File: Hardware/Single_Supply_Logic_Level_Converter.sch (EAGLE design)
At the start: 33 parts, among them U1 TXB0104, U2 TPS61200, U3 ADJ

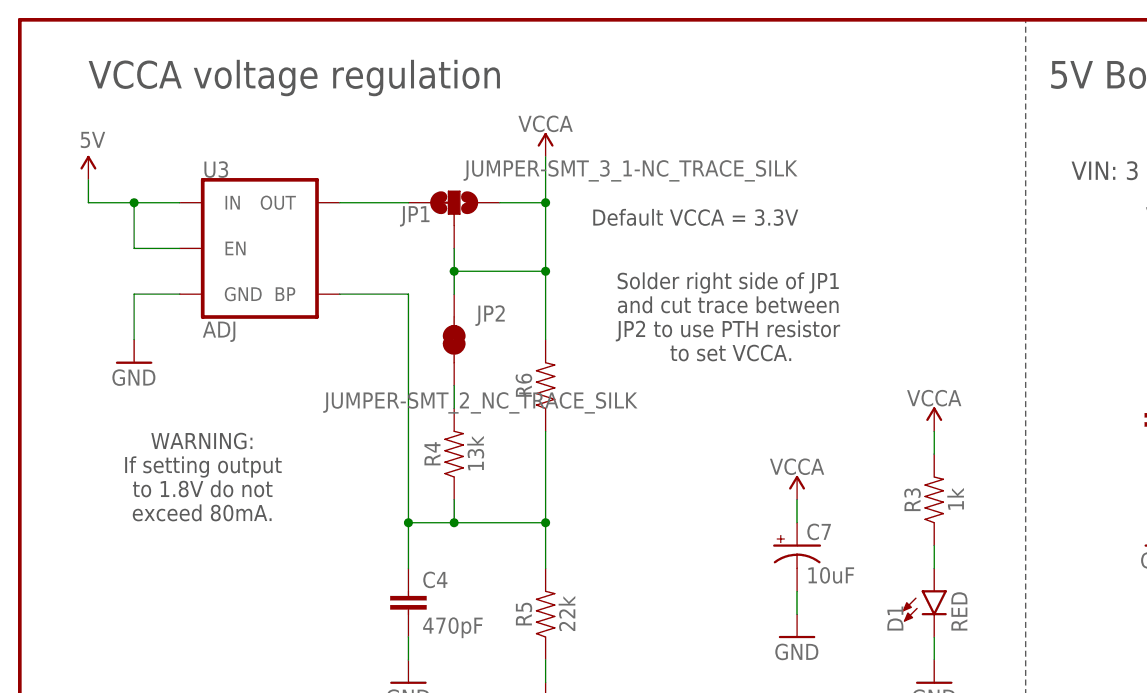
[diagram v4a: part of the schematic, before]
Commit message: changing voltage output programming
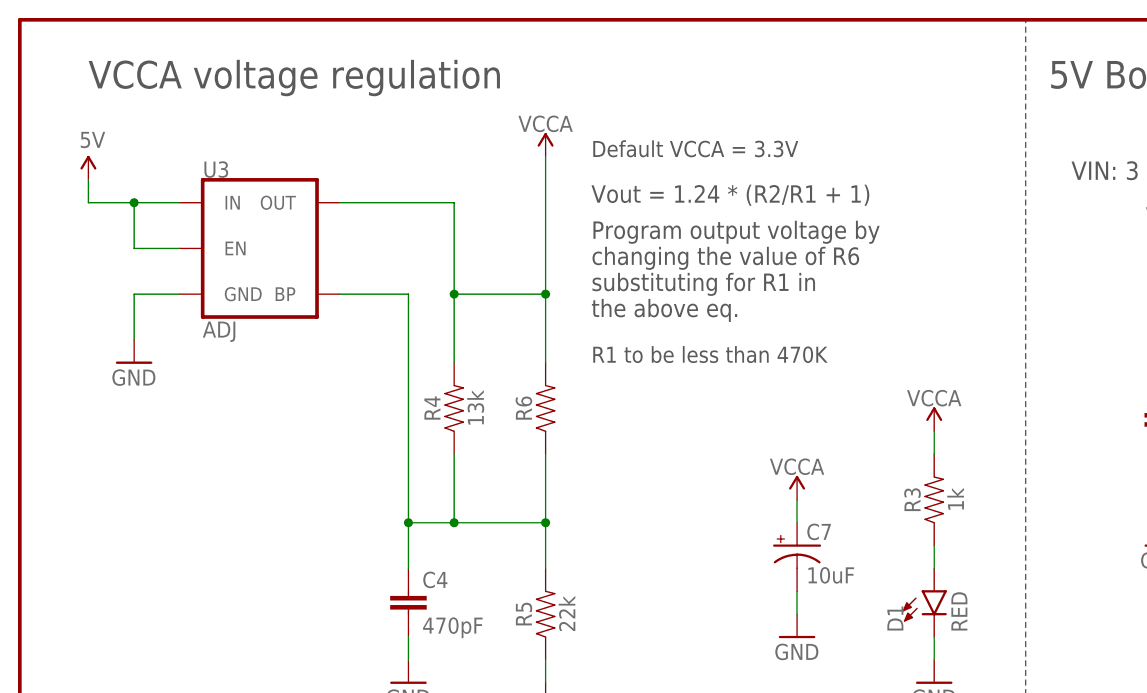
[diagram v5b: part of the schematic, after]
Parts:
- removed JP1: JUMPER-SMT_3_1-NC_TRACE_SILK, SparkFun-Jumpers:JUMPER-SMT_3_1-NC_TRACE_SILK
- removed JP2: JUMPER-SMT_2_NC_TRACE_SILK, SparkFun-Jumpers:JUMPER-SMT_2_NC_TRACE_SILK
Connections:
- removed net N$1: JP1.3, U3.OUT
- removed net N$12: JP2.1, R4.2
- net VCCA: now also R4.2, U3.OUT; no longer JP1.1, JP1.2, JP2.2
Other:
- note added: "Program output voltage by changing the value of R6 substituting for R1 in the above eq."
- note added: "R1 to be less than 470K"
- note added: "Vout = 1.24 * (R2/R1 + 1)"
- note removed: "Solder right side of JP1 and cut trace between JP2 to use PTH resistor to set VCCA."
- note removed: "WARNING: If setting output to 1.8V do not exceed 80mA."
- moved on the sheet: R4, R6
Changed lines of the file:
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@@
 <part name="R5" library="SparkFun-Resistors" deviceset="22KOHM" device="-0603-1/10W-1%" value="22k"/>
 <part name="R6" library="SparkFun-Resistors" deviceset="RESISTOR" device="AXIAL-0.3" value=" "/>
-<part name="JP1" library="SparkFun-Jumpers" deviceset="JUMPER-SMT_3_1-NC_TRACE" device="_SILK"/>
 <part name="GND5" library="SparkFun" deviceset="GND" device=""/>
 <part name="C4" library="SparkFun-Capacitors" deviceset="470PF" device="-0603-50V-5%" value="470pF"/>
 <part name="GND7" library="SparkFun" deviceset="GND" device=""/>
-<part name="JP2" library="SparkFun-Jumpers" deviceset="JUMPER-SMT_2_NC_TRACE" device="_SILK"/>
 <part name="U$1" library="SparkFun-PowerSymbols" deviceset="VCCA" device=""/>
 <part name="U$2" library="SparkFun-PowerSymbols" deviceset="VCCA" device=""/>
@@
 <wire x1="147.32" y1="96.52" x2="248.92" y2="96.52" width="0.1524" layer="97" style="shortdash"/>
 <wire x1="147.32" y1="35.56" x2="147.32" y2="96.52" width="0.1524" layer="97" style="shortdash"/>
-<text x="63.5" y="162.56" size="1.778" layer="97" font="vector" ratio="15">Default VCCA = 3.3V</text>
+<text x="63.5" y="170.18" size="1.778" layer="97" font="vector" ratio="15">Default VCCA = 3.3V</text>
 <text x="66.04" y="154.94" size="1.778" layer="97" font="vector" ratio="15"></text>
-<text x="78.74" y="152.4" size="1.778" layer="97" align="center">Solder right side of JP1
-and cut trace between
-JP2 to use PTH resistor
- to set VCCA. </text>
-<text x="20.32" y="134.62" size="1.778" layer="97" font="vector" ratio="15" align="center">WARNING:
-If setting output
-to 1.8V do not
-exceed 80mA. </text>
 <text x="12.7" y="88.9" size="3.048" layer="97" font="vector" ratio="15">Logic Level Conversion</text>
 <text x="7.62" y="177.8" size="3.048" layer="97" font="vector" ratio="15">VCCA voltage regulation</text>
 <text x="114.3" y="177.8" size="3.048" layer="97" font="vector" ratio="15">5V Boost Regulator</text>
+<text x="63.5" y="165.1" size="1.9304" layer="97" font="vector" ratio="15">Vout = 1.24 * (R2/R1 + 1)</text>
+<text x="63.5" y="147.32" size="1.778" layer="97" font="vector" ratio="15">R1 to be less than 470K</text>
+<text x="63.5" y="152.4" size="1.9304" layer="97" font="vector" ratio="15">Program output voltage by
+changing the value of R6
+substituting for R1 in
+the above eq.</text>
 </plain>
 <instances>
@@
 <instance part="U3" gate="U1" x="27.94" y="160.02"/>
 <instance part="GND1" gate="1" x="12.7" y="147.32"/>
-<instance part="R4" gate="G$1" x="48.26" y="137.16" rot="R90"/>
+<instance part="R4" gate="G$1" x="48.26" y="142.24" rot="R90"/>
 <instance part="R5" gate="G$1" x="58.42" y="119.38" rot="R90"/>
-<instance part="R6" gate="G$1" x="58.42" y="144.78" rot="R90"/>
-<instance part="JP1" gate="G$1" x="48.26" y="165.1" smashed="yes" rot="MR90">
-<attribute name="NAME" x="45.72" y="162.941" size="1.778" layer="95" font="vector" rot="MR0"/>
-<attribute name="VALUE" x="86.36" y="169.799" size="1.778" layer="96" font="vector" rot="MR0" align="top-left"/>
-</instance>
+<instance part="R6" gate="G$1" x="58.42" y="142.24" rot="R90"/>
 <instance part="GND5" gate="1" x="58.42" y="109.22"/>
 <instance part="C4" gate="G$1" x="43.18" y="119.38"/>
 <instance part="GND7" gate="1" x="43.18" y="111.76"/>
-<instance part="JP2" gate="G$1" x="48.26" y="149.86" smashed="yes" rot="R90">
-<attribute name="NAME" x="54.102" y="153.67" size="1.778" layer="95" font="vector" rot="R180"/>
-<attribute name="VALUE" x="68.58" y="142.24" size="1.778" layer="96" font="vector" rot="R180" align="top-left"/>
-</instance>
 <instance part="U$1" gate="G$1" x="58.42" y="170.18"/>
 <instance part="U$2" gate="G$1" x="78.74" y="73.66"/>
@@
 </segment>
 </net>
-<net name="N$1" class="0">
-<segment>
-<pinref part="U3" gate="U1" pin="OUT"/>
-<pinref part="JP1" gate="G$1" pin="3"/>
-<wire x1="35.56" y1="165.1" x2="43.18" y2="165.1" width="0.1524" layer="91"/>
-</segment>
-</net>
 <net name="N$11" class="0">
 <segment>
-<wire x1="58.42" y1="139.7" x2="58.42" y2="129.54" width="0.1524" layer="91"/>
+<wire x1="58.42" y1="137.16" x2="58.42" y2="129.54" width="0.1524" layer="91"/>
 <pinref part="R4" gate="G$1" pin="1"/>
 <pinref part="R5" gate="G$1" pin="2"/>
-<wire x1="48.26" y1="132.08" x2="48.26" y2="129.54" width="0.1524" layer="91"/>
+<wire x1="48.26" y1="137.16" x2="48.26" y2="129.54" width="0.1524" layer="91"/>
 <pinref part="U3" gate="U1" pin="BP"/>
 <wire x1="48.26" y1="129.54" x2="58.42" y2="129.54" width="0.1524" layer="91"/>
@@
 </segment>
 </net>
-<net name="N$12" class="0">
-<segment>
+<net name="VCCA" class="0">
+<segment>
+<pinref part="R6" gate="G$1" pin="2"/>
+<wire x1="58.42" y1="147.32" x2="58.42" y2="154.94" width="0.1524" layer="91"/>
+<pinref part="U$1" gate="G$1" pin="VCCA"/>
 <pinref part="R4" gate="G$1" pin="2"/>
-<pinref part="JP2" gate="G$1" pin="1"/>
-<wire x1="48.26" y1="142.24" x2="48.26" y2="144.78" width="0.1524" layer="91"/>
-</segment>
-</net>
-<net name="VCCA" class="0">
-<segment>
-<pinref part="JP2" gate="G$1" pin="2"/>
-<pinref part="JP1" gate="G$1" pin="2"/>
-<wire x1="48.26" y1="154.94" x2="48.26" y2="157.48" width="0.1524" layer="91"/>
-<pinref part="JP1" gate="G$1" pin="1"/>
-<wire x1="48.26" y1="157.48" x2="48.26" y2="160.02" width="0.1524" layer="91"/>
-<wire x1="53.34" y1="165.1" x2="58.42" y2="165.1" width="0.1524" layer="91"/>
-<pinref part="R6" gate="G$1" pin="2"/>
-<wire x1="58.42" y1="149.86" x2="58.42" y2="157.48" width="0.1524" layer="91"/>
-<wire x1="58.42" y1="157.48" x2="58.42" y2="165.1" width="0.1524" layer="91"/>
-<wire x1="48.26" y1="157.48" x2="58.42" y2="157.48" width="0.1524" layer="91"/>
-<junction x="48.26" y="157.48"/>
-<junction x="58.42" y="157.48"/>
-<wire x1="58.42" y1="165.1" x2="58.42" y2="170.18" width="0.1524" layer="91"/>
-<pinref part="U$1" gate="G$1" pin="VCCA"/>
-<junction x="58.42" y="165.1"/>
-</segment>
-<segment>
+<wire x1="58.42" y1="154.94" x2="58.42" y2="170.18" width="0.1524" layer="91"/>
+<wire x1="48.26" y1="147.32" x2="48.26" y2="154.94" width="0.1524" layer="91"/>
+<wire x1="48.26" y1="154.94" x2="58.42" y2="154.94" width="0.1524" layer="91"/>
+<wire x1="48.26" y1="154.94" x2="48.26" y2="165.1" width="0.1524" layer="91"/>
+<pinref part="U3" gate="U1" pin="OUT"/>
+<wire x1="35.56" y1="165.1" x2="48.26" y2="165.1" width="0.1524" layer="91"/>
+<junction x="48.26" y="154.94"/>
+<junction x="58.42" y="154.94"/>
+</segment>
+<segment>

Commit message: Updated per QC review
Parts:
- R1: value 200k -> (none); device SparkFun-Resistors:200KOHM-0603-1/10W-1% -> SparkFun-Resistors:RESISTORAXIAL-0.3
- R2: value 1.8M -> 22k; device SparkFun-Resistors:1.8MOHM -> SparkFun-Resistors:22KOHM-0603-1/10W-1%
- R3: value 1k -> 13k; device SparkFun-Resistors:1KOHM-0603-1/10W-1% -> SparkFun-Resistors:13KOHM-0603-1/10W-1%
- R4: value 13k -> 1k; device SparkFun-Resistors:13KOHM-0603-1/10W-1% -> SparkFun-Resistors:1KOHM-0603-1/10W-1%
- R5: value 22k -> 1.8M; device SparkFun-Resistors:22KOHM-0603-1/10W-1% -> SparkFun-Resistors:1.8MOHM
- R6: value (none) -> 200k; device SparkFun-Resistors:RESISTORAXIAL-0.3 -> SparkFun-Resistors:200KOHM-0603-1/10W-1%
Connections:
- net 5V: now also R5.2; no longer R2.2
- net FB: now also R5.1, R6.2; no longer R1.2, R2.1
- net GND: now also R2.1, R6.1; no longer R1.1, R5.1
- net N$11: now also R1.1, R2.2, R3.1; no longer R4.1, R5.2, R6.1
- net N$3: now also R4.1; no longer R3.1
- net VCCA: now also R1.2; no longer R6.2
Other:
- moved on the sheet: R1, R2, R3, R4, R5, R6
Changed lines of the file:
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@@
 <part name="FRAME1" library="SparkFun-Aesthetics" deviceset="FRAME-LETTER" device=""/>
 <part name="SUPPLY5" library="SparkFun-Aesthetics" deviceset="5V" device=""/>
-<part name="R1" library="SparkFun-Resistors" deviceset="200KOHM" device="-0603-1/10W-1%" value="200k"/>
-<part name="R2" library="SparkFun-Resistors" deviceset="1.8MOHM" device="" value="1.8M"/>
+<part name="R6" library="SparkFun-Resistors" deviceset="200KOHM" device="-0603-1/10W-1%" value="200k"/>
+<part name="R5" library="SparkFun-Resistors" deviceset="1.8MOHM" device="" value="1.8M"/>
 <part name="GND8" library="SparkFun" deviceset="GND" device=""/>
 <part name="SUPPLY6" library="SparkFun-Aesthetics" deviceset="5V" device=""/>
@@
 <part name="U3" library="SparkFun-IC-Power" deviceset="V_REG_MIC5205" device="ADJ" value="ADJ"/>
 <part name="GND1" library="SparkFun" deviceset="GND" device=""/>
-<part name="R4" library="SparkFun-Resistors" deviceset="13KOHM" device="-0603-1/10W-1%" value="13k"/>
-<part name="R5" library="SparkFun-Resistors" deviceset="22KOHM" device="-0603-1/10W-1%" value="22k"/>
-<part name="R6" library="SparkFun-Resistors" deviceset="RESISTOR" device="AXIAL-0.3" value=" "/>
+<part name="R3" library="SparkFun-Resistors" deviceset="13KOHM" device="-0603-1/10W-1%" value="13k"/>
+<part name="R2" library="SparkFun-Resistors" deviceset="22KOHM" device="-0603-1/10W-1%" value="22k"/>
+<part name="R1" library="SparkFun-Resistors" deviceset="RESISTOR" device="AXIAL-0.3" value=" "/>
 <part name="GND5" library="SparkFun" deviceset="GND" device=""/>
 <part name="C4" library="SparkFun-Capacitors" deviceset="470PF" device="-0603-50V-5%" value="470pF"/>
@@
 <part name="U$5" library="SparkFun-PowerSymbols" deviceset="VCCA" device=""/>
 <part name="D1" library="SparkFun-LED" deviceset="LED-RED" device="0603" value="RED"/>
-<part name="R3" library="SparkFun-Resistors" deviceset="1KOHM" device="-0603-1/10W-1%" value="1k"/>
+<part name="R4" library="SparkFun-Resistors" deviceset="1KOHM" device="-0603-1/10W-1%" value="1k"/>
 <part name="GND10" library="SparkFun" deviceset="GND" device=""/>
 <part name="U$6" library="SparkFun-PowerSymbols" deviceset="VCCA" device=""/>
@@
 <instance part="FRAME1" gate="V" x="147.32" y="0"/>
 <instance part="SUPPLY5" gate="G$1" x="223.52" y="147.32"/>
-<instance part="R1" gate="G$1" x="213.36" y="121.92" rot="R90"/>
-<instance part="R2" gate="G$1" x="213.36" y="137.16" rot="R90"/>
+<instance part="R6" gate="G$1" x="213.36" y="121.92" rot="R90"/>
+<instance part="R5" gate="G$1" x="213.36" y="137.16" rot="R90"/>
 <instance part="GND8" gate="1" x="127" y="127"/>
 <instance part="SUPPLY6" gate="G$1" x="7.62" y="167.64"/>
@@
 <instance part="U3" gate="U1" x="27.94" y="160.02"/>
 <instance part="GND1" gate="1" x="12.7" y="147.32"/>
-<instance part="R4" gate="G$1" x="48.26" y="142.24" rot="R90"/>
-<instance part="R5" gate="G$1" x="58.42" y="119.38" rot="R90"/>
-<instance part="R6" gate="G$1" x="58.42" y="142.24" rot="R90"/>
+<instance part="R3" gate="G$1" x="48.26" y="142.24" rot="R90"/>
+<instance part="R2" gate="G$1" x="58.42" y="119.38" rot="R90"/>
+<instance part="R1" gate="G$1" x="58.42" y="142.24" rot="R90"/>
 <instance part="GND5" gate="1" x="58.42" y="109.22"/>
 <instance part="C4" gate="G$1" x="43.18" y="119.38"/>
@@
 <instance part="U$5" gate="G$1" x="86.36" y="132.08"/>
 <instance part="D1" gate="G$1" x="101.6" y="121.92"/>
-<instance part="R3" gate="G$1" x="101.6" y="132.08" rot="R90"/>
+<instance part="R4" gate="G$1" x="101.6" y="132.08" rot="R90"/>
 <instance part="GND10" gate="1" x="101.6" y="111.76"/>
 <instance part="U$6" gate="G$1" x="101.6" y="139.7"/>
@@
 <pinref part="U2" gate="G$1" pin="VOUT"/>
 <pinref part="SUPPLY5" gate="G$1" pin="5V"/>
-<pinref part="R2" gate="G$1" pin="2"/>
+<pinref part="R5" gate="G$1" pin="2"/>
 <wire x1="213.36" y1="142.24" x2="213.36" y2="144.78" width="0.1524" layer="91"/>
 <junction x="213.36" y="144.78"/>
@@
 <junction x="223.52" y="114.3"/>
 <wire x1="223.52" y1="114.3" x2="213.36" y2="114.3" width="0.1524" layer="91"/>
-<pinref part="R1" gate="G$1" pin="1"/>
+<pinref part="R6" gate="G$1" pin="1"/>
 <wire x1="213.36" y1="116.84" x2="213.36" y2="114.3" width="0.1524" layer="91"/>
 <junction x="213.36" y="114.3"/>
@@
 </segment>
 <segment>
-<pinref part="R5" gate="G$1" pin="1"/>
+<pinref part="R2" gate="G$1" pin="1"/>
 <wire x1="58.42" y1="114.3" x2="58.42" y2="111.76" width="0.1524" layer="91"/>
 <pinref part="GND5" gate="1" pin="GND"/>
@@
 <wire x1="187.96" y1="139.7" x2="193.04" y2="139.7" width="0.1524" layer="91"/>
 <wire x1="193.04" y1="139.7" x2="193.04" y2="129.54" width="0.1524" layer="91"/>
-<pinref part="R2" gate="G$1" pin="1"/>
-<pinref part="R1" gate="G$1" pin="2"/>
+<pinref part="R5" gate="G$1" pin="1"/>
+<pinref part="R6" gate="G$1" pin="2"/>
 <wire x1="213.36" y1="132.08" x2="213.36" y2="129.54" width="0.1524" layer="91"/>
 <wire x1="213.36" y1="129.54" x2="213.36" y2="127" width="0.1524" layer="91"/>
@@
 <segment>
 <wire x1="58.42" y1="137.16" x2="58.42" y2="129.54" width="0.1524" layer="91"/>
-<pinref part="R4" gate="G$1" pin="1"/>
-<pinref part="R5" gate="G$1" pin="2"/>
+<pinref part="R3" gate="G$1" pin="1"/>
+<pinref part="R2" gate="G$1" pin="2"/>
 <wire x1="48.26" y1="137.16" x2="48.26" y2="129.54" width="0.1524" layer="91"/>
 <pinref part="U3" gate="U1" pin="BP"/>
@@
 <junction x="43.18" y="129.54"/>
 <junction x="58.42" y="129.54"/>
-<pinref part="R6" gate="G$1" pin="1"/>
+<pinref part="R1" gate="G$1" pin="1"/>
 </segment>
 </net>
 <net name="VCCA" class="0">
 <segment>
-<pinref part="R6" gate="G$1" pin="2"/>
+<pinref part="R1" gate="G$1" pin="2"/>
 <wire x1="58.42" y1="147.32" x2="58.42" y2="154.94" width="0.1524" layer="91"/>
 <pinref part="U$1" gate="G$1" pin="VCCA"/>
-<pinref part="R4" gate="G$1" pin="2"/>
+<pinref part="R3" gate="G$1" pin="2"/>
 <wire x1="58.42" y1="154.94" x2="58.42" y2="170.18" width="0.1524" layer="91"/>
 <wire x1="48.26" y1="147.32" x2="48.26" y2="154.94" width="0.1524" layer="91"/>
@@
 </segment>
 <segment>
-<pinref part="R3" gate="G$1" pin="2"/>
+<pinref part="R4" gate="G$1" pin="2"/>
 <wire x1="101.6" y1="137.16" x2="101.6" y2="139.7" width="0.1524" layer="91"/>
 <pinref part="U$6" gate="G$1" pin="VCCA"/>
@@
 <net name="N$3" class="0">
 <segment>
-<pinref part="R3" gate="G$1" pin="1"/>
+<pinref part="R4" gate="G$1" pin="1"/>
 <pinref part="D1" gate="G$1" pin="A"/>
 <wire x1="101.6" y1="127" x2="101.6" y2="124.46" width="0.1524" layer="91"/>

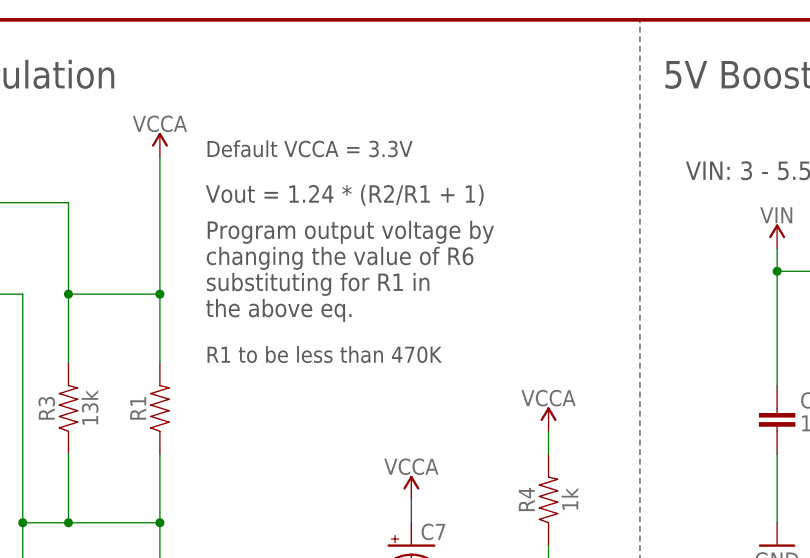
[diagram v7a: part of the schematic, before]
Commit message: Updating schematic notes to include resistor values for VOUT programming
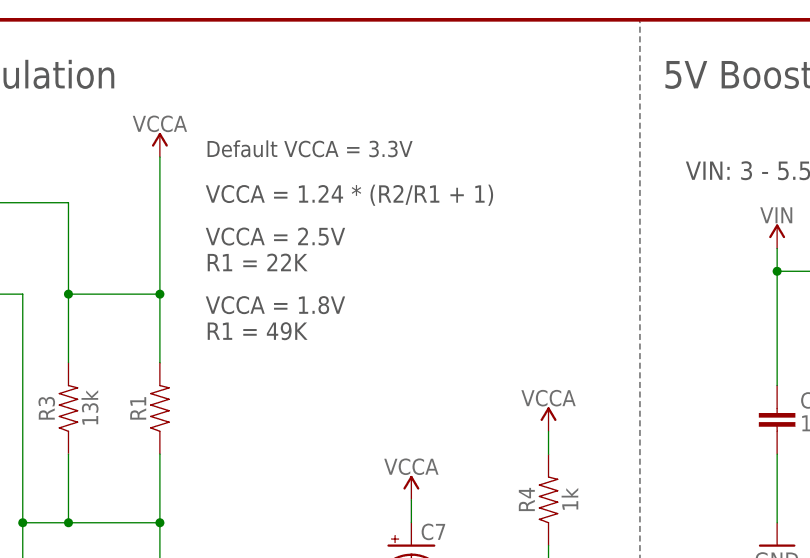
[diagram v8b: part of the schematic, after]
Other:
- note added: "VCCA = 1.24 * (R2/R1 + 1)"
- note added: "VCCA = 1.8V R1 = 49K"
- note added: "VCCA = 2.5V R1 = 22K"
- note removed: "Program output voltage by changing the value of R6 substituting for R1 in the above eq."
- note removed: "R1 to be less than 470K"
- note removed: "Vout = 1.24 * (R2/R1 + 1)"
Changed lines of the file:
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@@
 <text x="7.62" y="177.8" size="3.048" layer="97" font="vector" ratio="15">VCCA voltage regulation</text>
 <text x="114.3" y="177.8" size="3.048" layer="97" font="vector" ratio="15">5V Boost Regulator</text>
-<text x="63.5" y="165.1" size="1.9304" layer="97" font="vector" ratio="15">Vout = 1.24 * (R2/R1 + 1)</text>
-<text x="63.5" y="147.32" size="1.778" layer="97" font="vector" ratio="15">R1 to be less than 470K</text>
-<text x="63.5" y="152.4" size="1.9304" layer="97" font="vector" ratio="15">Program output voltage by
-changing the value of R6
-substituting for R1 in
-the above eq.</text>
+<text x="63.5" y="165.1" size="1.9304" layer="97" font="vector" ratio="15">VCCA = 1.24 * (R2/R1 + 1)</text>
+<text x="63.5" y="152.4" size="1.9304" layer="97" font="vector" ratio="15"></text>
+<text x="63.5" y="157.48" size="1.9304" layer="97" font="vector" ratio="15">VCCA = 2.5V
+R1 = 22K</text>
+<text x="63.5" y="149.86" size="1.9304" layer="97" font="vector" ratio="15">VCCA = 1.8V
+R1 = 49K</text>
 </plain>
 <instances>
